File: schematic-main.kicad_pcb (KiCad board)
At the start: 2 copper layers, 100 x 99.9 mm, 123 parts, among them IC1 AD8544ARUZ-REEL, IC2 LM76202QPWPRQ1, J1 Battery, J10 Motor, J2 CAN, J3 V_P, J4 Conn_01x04, J7 C_P, J8 VALVE, J9 PURGE_VALVE, P1 USB_C_Plug_USB2.0, U2 TPS62933, U3 USBLC6-2P6, U4 ESP32-S3FN8, U5 SN65HVD232, U6 DRV8801PWP, Y1 Crystal_GND24

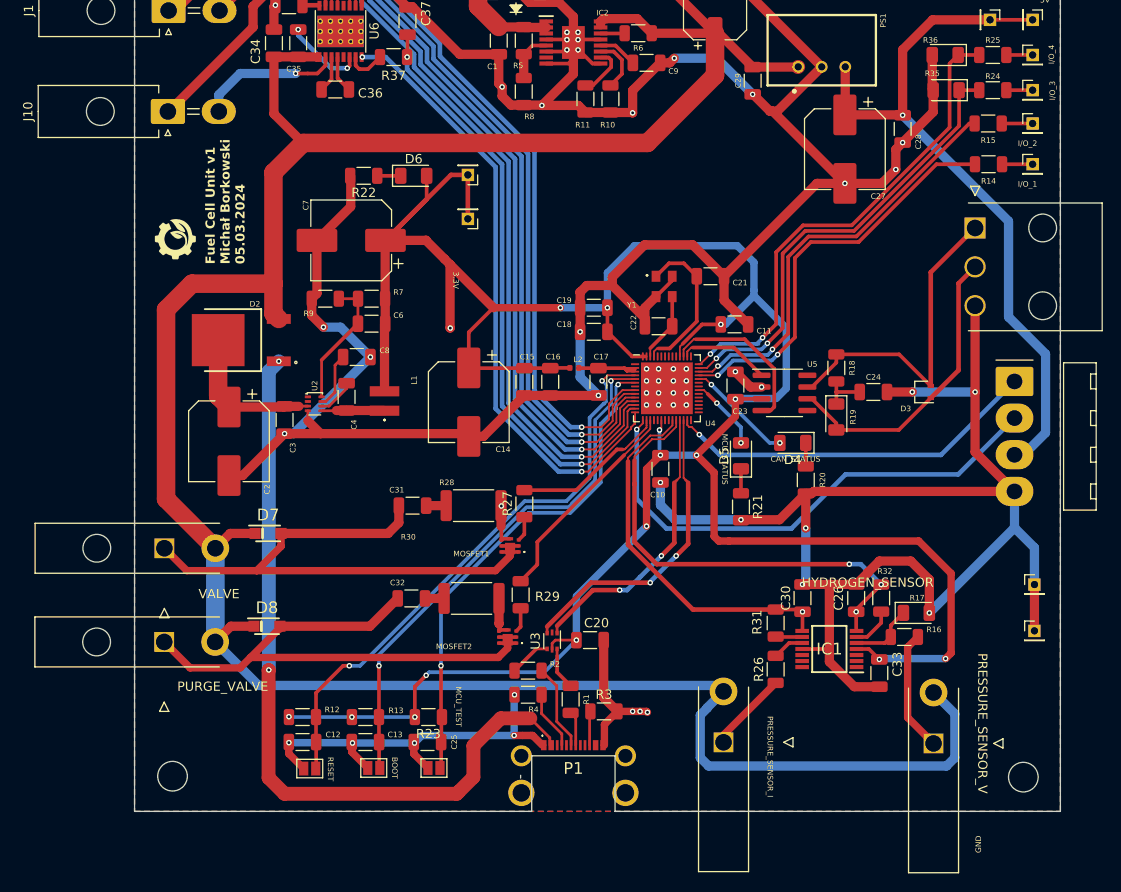
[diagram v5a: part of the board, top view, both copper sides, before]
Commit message: Change of PRESSURE_SENSOR_I circuit
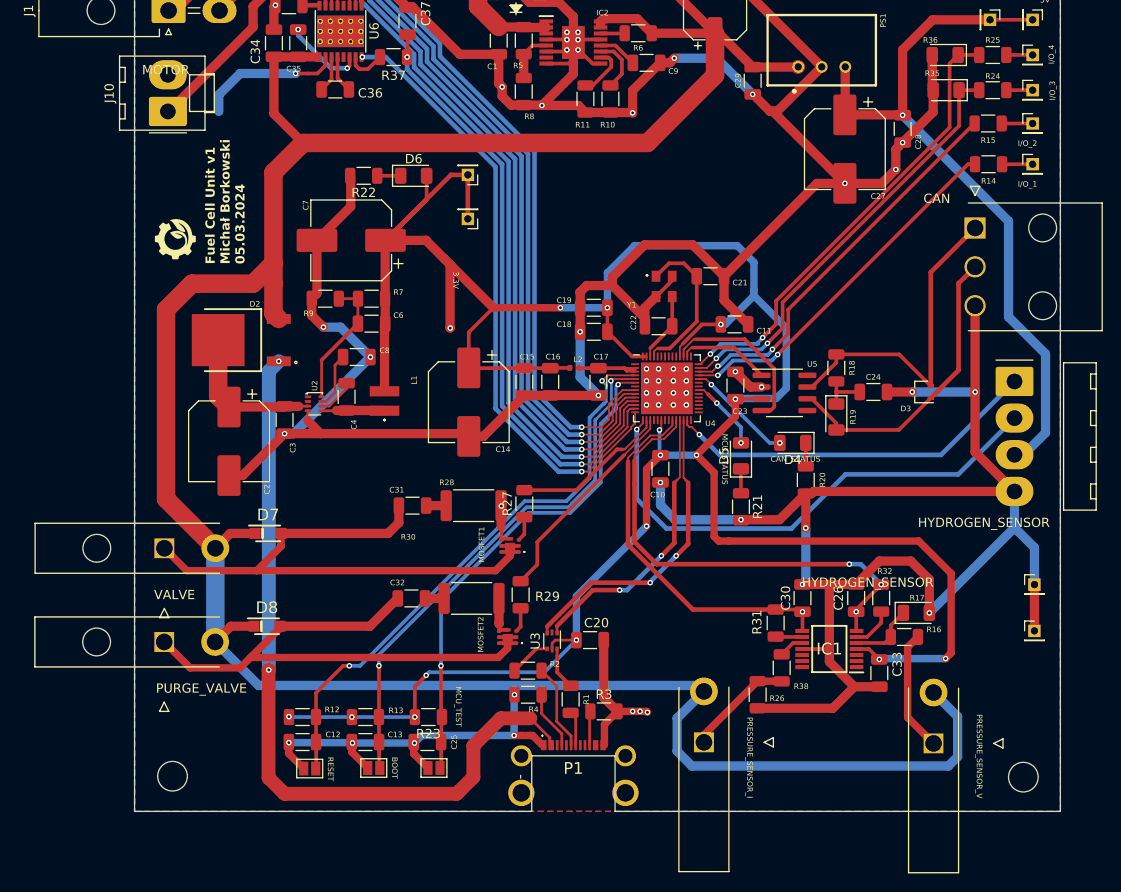
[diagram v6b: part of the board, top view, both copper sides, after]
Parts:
- added R38: 0, Resistor_SMD:R_1206_3216Metric, F.Cu at (118.9, 136.3)
- J10: footprint Connector_Molex:Molex_Mini-Fit_Jr_5569-02A2_2x01_P4.20mm_Horizontal -> Connector_Molex:Molex_KK-396_A-41791-0002_1x02_P3.96mm_Vertical
- moved R26 3.36 mm to (116.3, 139.2)
- moved J7 2.12 mm to (110.5, 144.3)
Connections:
- R26 pad 1: /IO/PRESSURE_SENSOR_I -> GND
- R26 pad 2: Net-(IC1-+IN_C) -> /IO/PRESSURE_SENSOR_I
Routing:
- net GND: track 551.9 -> 563.4 mm
- net /I/O_1_MCU: track 44.3 -> 39.3 mm
- net /I/O_2_MCU: track 45.8 -> 42.5 mm
- net /I/O_4_MCU: track 53.0 -> 49.9 mm
- net /I/O_3_MCU: track 49.7 -> 46.7 mm
- net /IO/PRESSURE_SENSOR_I: track 8.75 -> 11.7 mm
- net +12V: track 324.4 -> 325.9 mm
- net Net-(IC1-+IN_C): track 3.46 -> 2.72 mm
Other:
- board text added: "CAN"
- board text added: "MOTOR"
- board text removed: "GND"

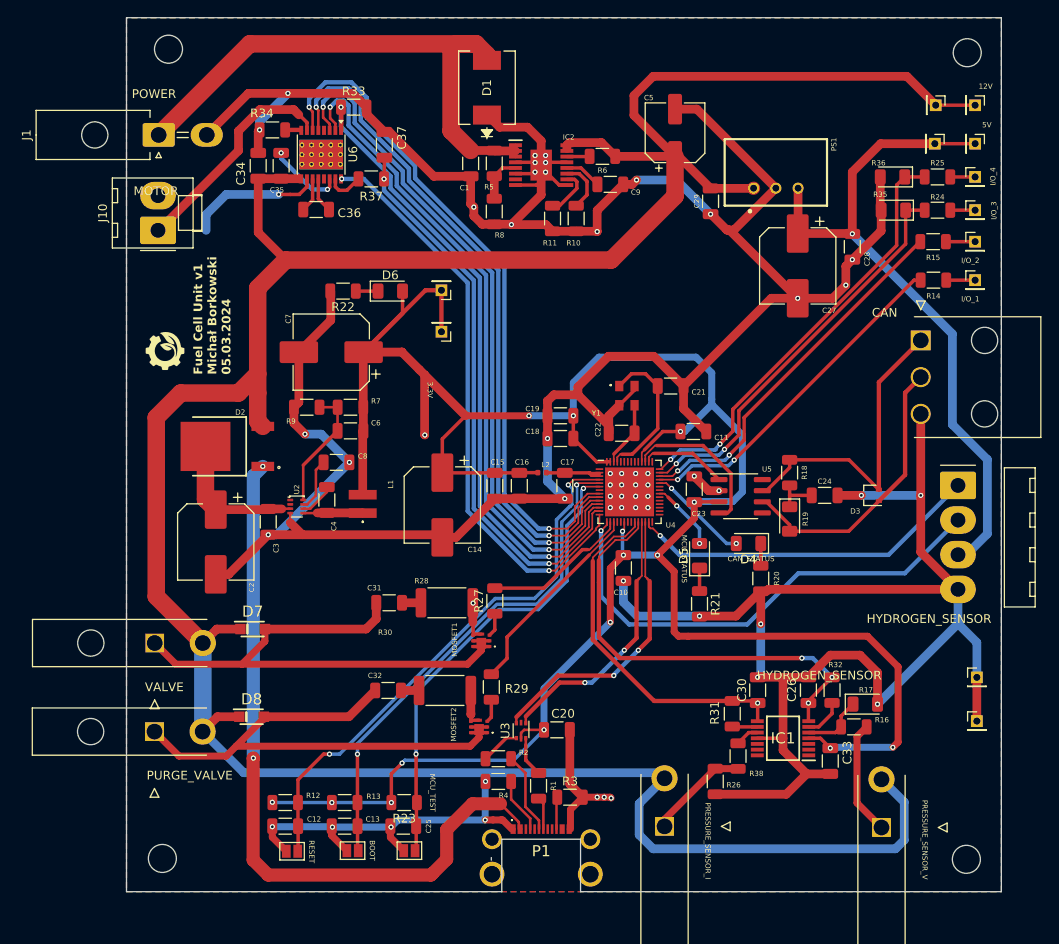
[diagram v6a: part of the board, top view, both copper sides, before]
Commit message: Change of signatures
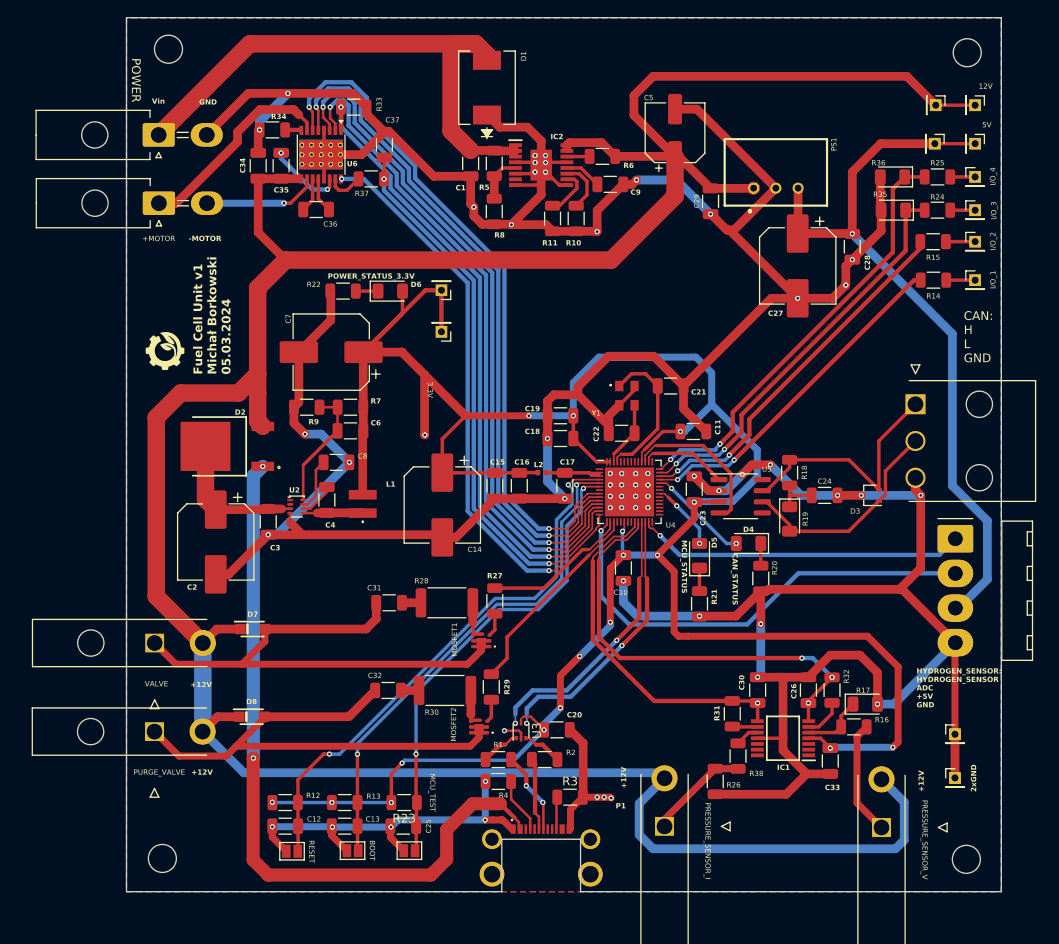
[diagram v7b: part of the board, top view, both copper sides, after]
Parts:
- J10: footprint Connector_Molex:Molex_KK-396_A-41791-0002_1x02_P3.96mm_Vertical -> Connector_Molex:Molex_Mini-Fit_Jr_5569-02A2_2x01_P4.20mm_Horizontal
- moved J2 7.32 mm to (139.2, 96.1)
- moved TP1 6.96 mm to (143.7, 133.8)
- moved TP2 6.96 mm to (143.7, 138.8)
- moved J4 6.11 mm to (143.7, 111.5)
- moved R1 5.49 mm to (91.5, 136.7), turned to 180 degrees
- moved R2 5.30 mm to (96.8, 136.7), turned to 0 degrees
- moved J10 3.10 mm to (52.7, 73.1)
- turned U3 to 90 degrees
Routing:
- net GND: track 563.4 -> 589.4 mm, vias 55 -> 58
- net /IO/CANH: track 35.9 -> 28.3 mm
- net /IO/CANL: track 32.7 -> 25.2 mm
- net +5V: track 78.9 -> 84.8 mm
- net Net-(P1-D-): track 3.72 -> 9.48 mm, vias 0 -> 2
- net /HYDROGEN_SENSOR_: track 41.2 -> 37.7 mm
- net /HYDROGEN_SENSOR_ADC: track 55.8 -> 53.0 mm
- net /IO_2/-MOTOR: track 15.5 -> 13.1 mm
- net /MCU/USB_D+: track 37.9 -> 35.6 mm
- net /IO_2/+MOTOR: track 25.6 -> 23.5 mm
- net +3.3V: track 295.0 -> 296.8 mm, vias 16 -> 18
- net Net-(P1-D+): track 9.37 -> 8.29 mm
- net /MCU/USB_D-: track 35.3 -> 35.8 mm
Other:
- outline, holes or cut-outs redrawn
- board text added: "+12V"
- board text added: "+MOTOR"
- board text added: "-MOTOR"
- board text added: "2xGND"
- board text added: "CAN: H L GND"
- board text added: "GND"
- board text added: "HYDROGEN_SENSOR: HYDROGEN_SENSOR ADC +5V GND"
- board text added: "POWER_STATUS_3.3V"
- board text added: "Vin"
- board text removed: "CAN"
- board text removed: "HYDROGEN_SENSOR"
- board text removed: "MOTOR"

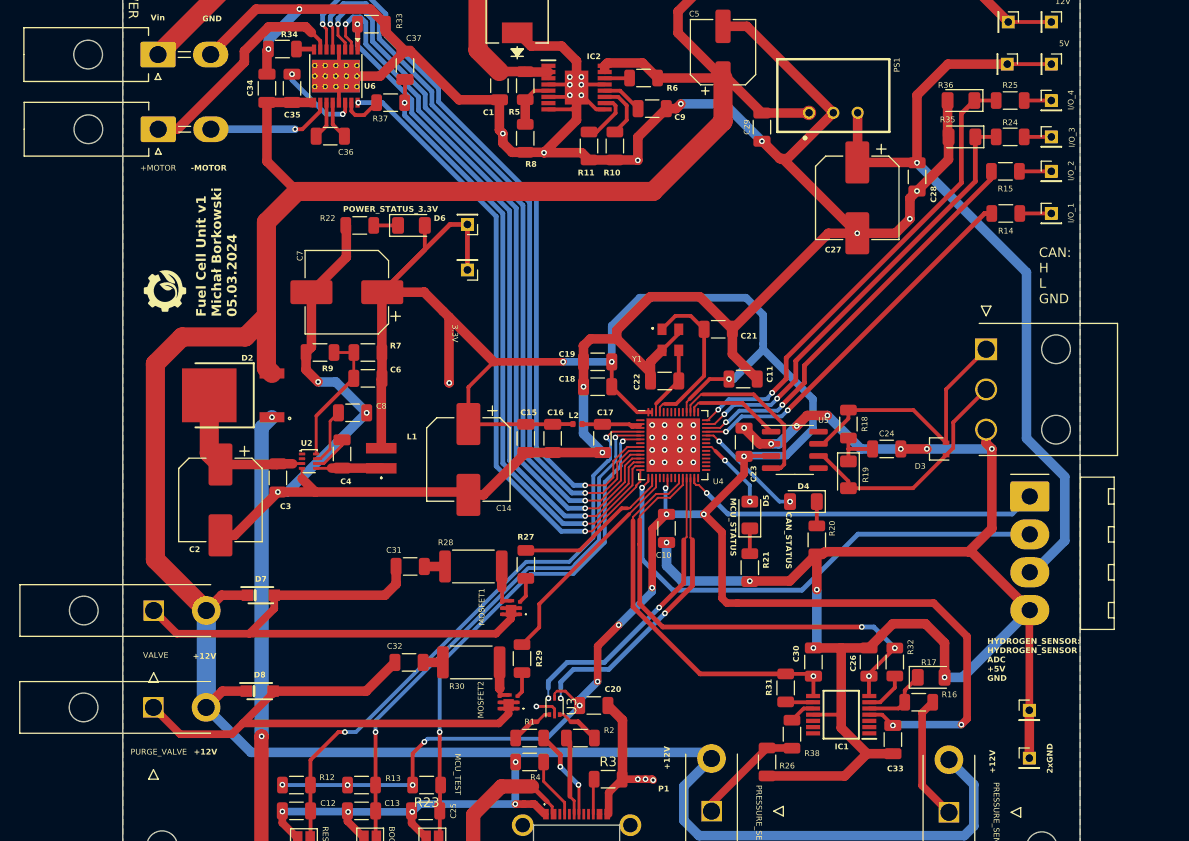
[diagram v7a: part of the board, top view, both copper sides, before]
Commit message: Change of socket for Hudrogen sensor
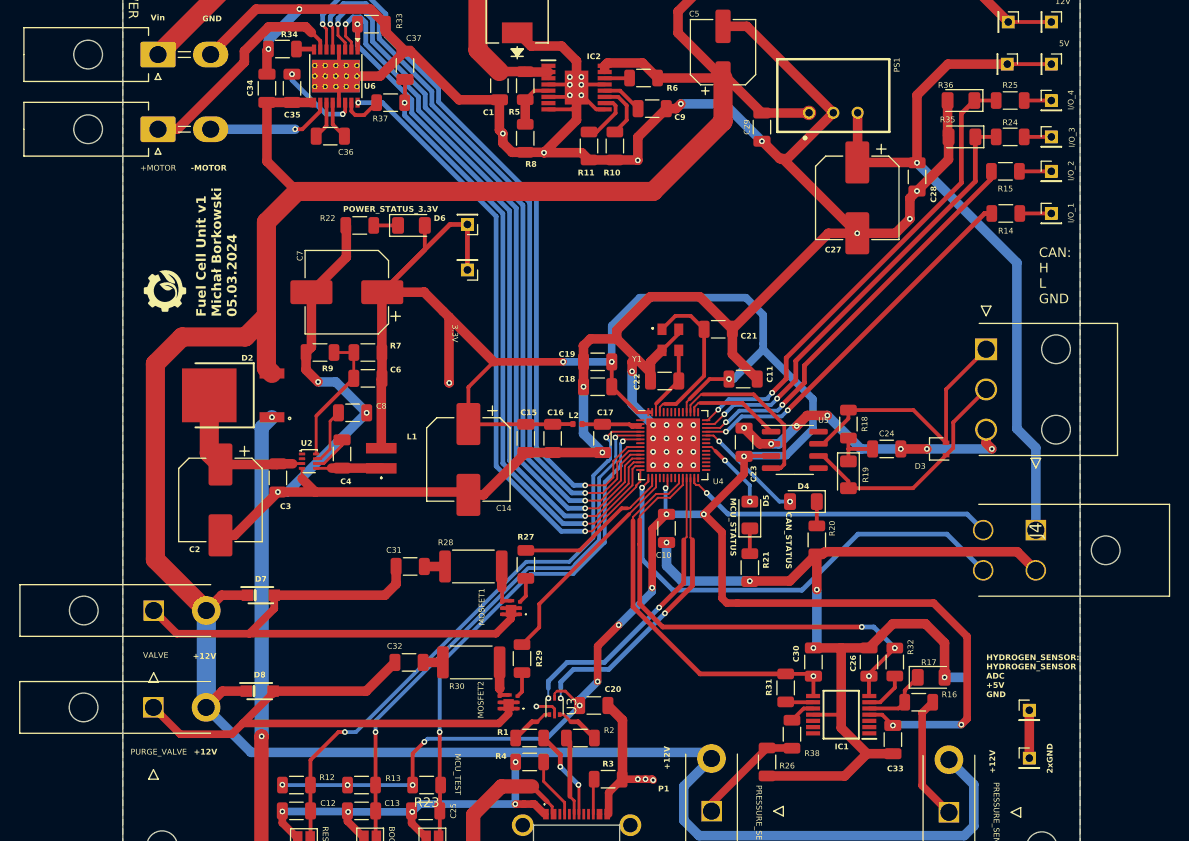
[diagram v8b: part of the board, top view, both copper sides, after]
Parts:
- J4: footprint Connector_Molex:Molex_KK-396_A-41792-0004_1x04_P3.96mm_Horizontal -> Lib:39-30-104Y
- moved J4 3.58 mm to (144.4, 115.0), turned to 90 degrees
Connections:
- J4 pad 1: /HYDROGEN_SENSOR_ -> +5V
- J4 pad 2: /HYDROGEN_SENSOR_ADC -> GND
- J4 pad 3: +5V -> /HYDROGEN_SENSOR_
- J4 pad 4: GND -> /HYDROGEN_SENSOR_ADC
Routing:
- net GND: track 589.4 -> 564.7 mm, vias 58 -> 59
- net +5V: track 84.8 -> 77.4 mm
- net /HYDROGEN_SENSOR_: track 37.7 -> 32.7 mm
- net /HYDROGEN_SENSOR_ADC: track 53.0 -> 49.7 mm
